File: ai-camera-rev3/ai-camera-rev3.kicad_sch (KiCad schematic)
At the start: 176 parts, among them J1 Conn-01x02_P2mm_NONAME_JST-PH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, J2 TYPE-C-31-M-12, J3 MAXLAB, J4 Conn-02x10_P2.54mm_B-2100S20P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, J5 Conn-01x02_P1.25mm_10114829-1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, J6 Conn_01x24_FFC_0.5mm_AFC01-S2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, Q1 2N7002, Q10 2N7002, Q2 2N7002, Q3 AO3401A, Q4 AO3401A, Q5 2N7002, Q6 AO3401A, Q7 2N7002, Q8 AO3401A, Q9 2N7002, SW1 SW_PB_90deg_K2-1102AQ-H4CW-01, SW2 SW_PB_TS-1187A-B-A-B, SW3 SW_PB_TS-1187A-B-A-B, SW4 SW_PB_90deg_K2-1102AQ-H4CW-01, U1 TP4057-42-SOT26-R, U10 ESP32-S3-WROOM-1-N16R8, U11 MT9284-28J, U12 LTR-303ALS-01, U2 XC6206-2.8V, U3 PCF85063AT_SO8, U4 SOT-23-6_SN74LVC1G373DBVR_TI, U5 SY8089AAAC, U6 PIR_AS312, U7 XC6206-2.8V, U8 RT9166-12GVL, U9 AP1511B, Y1 32.768kHz_Q13FC1350000400

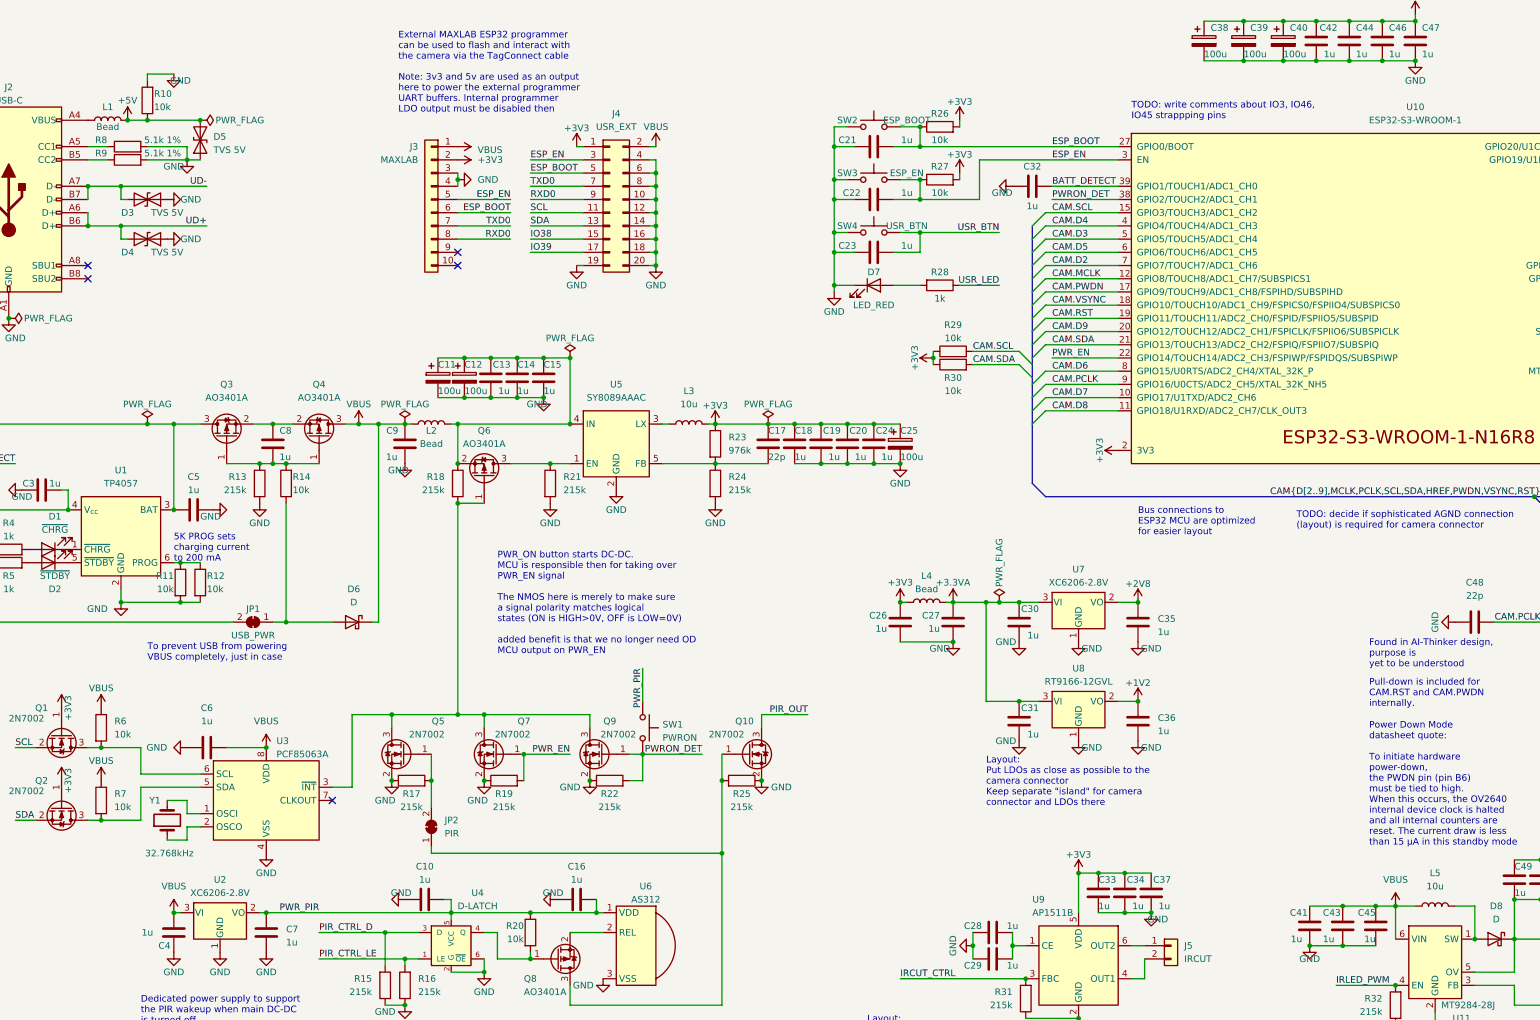
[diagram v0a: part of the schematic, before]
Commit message: EAC-60: rev3: fix all errors and warnings from 7.0.2 KiCAD, update to newer KIML
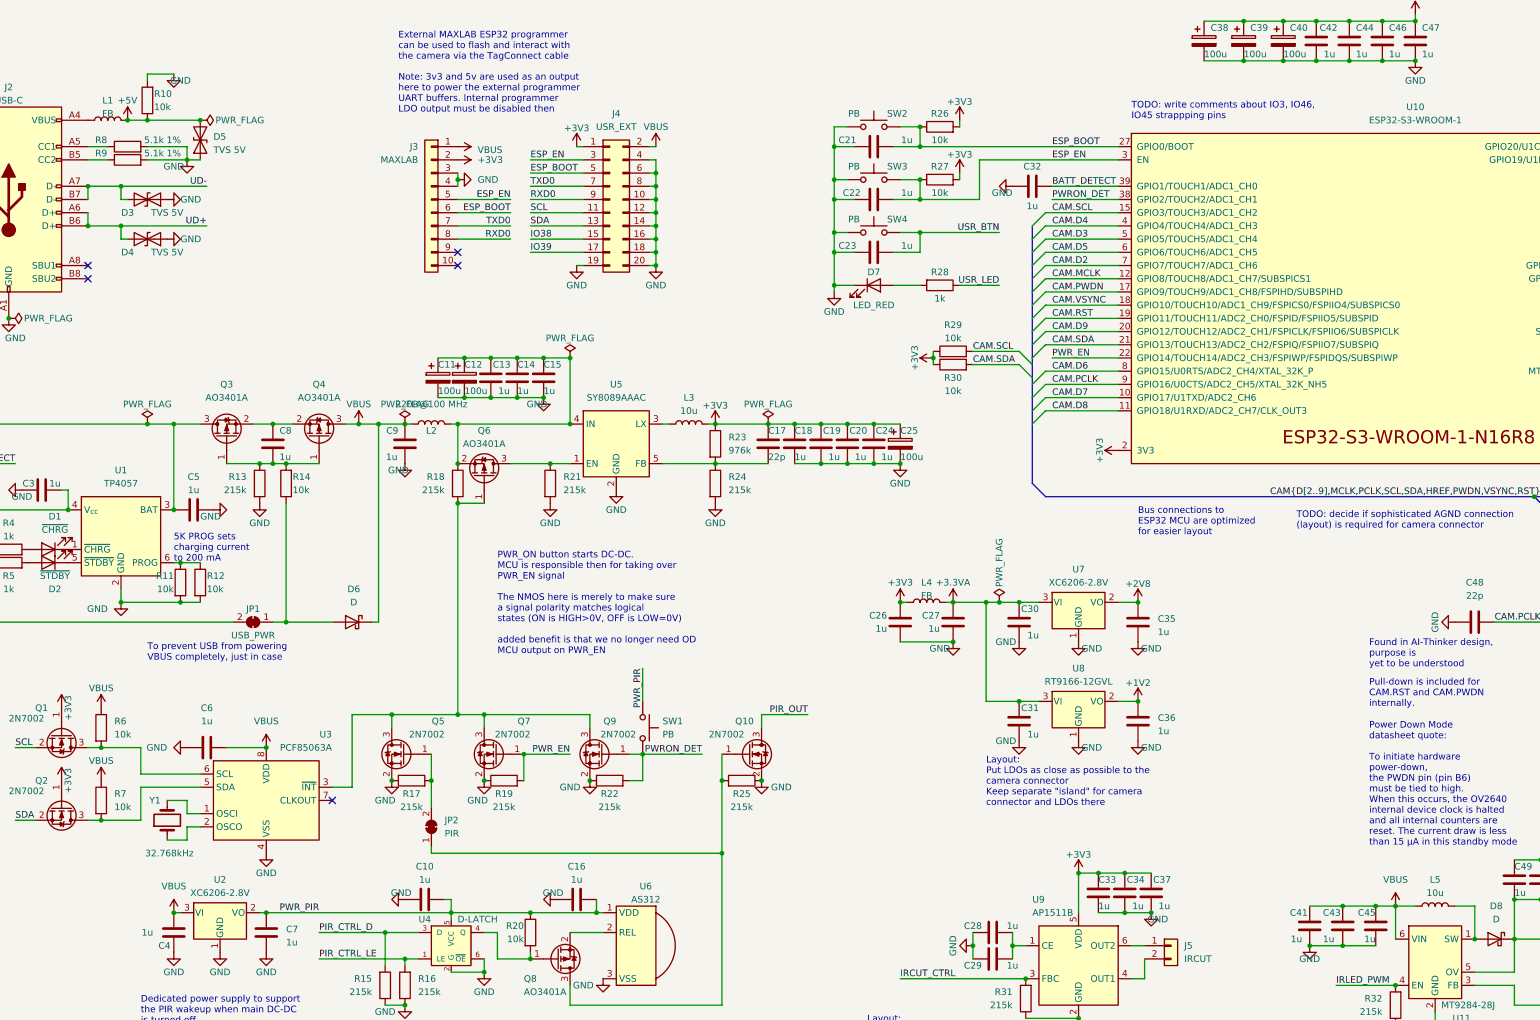
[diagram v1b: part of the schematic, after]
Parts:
- D6, D8: Rating (none) -> 1A
- L1, L4: value 0805_FB_220R@100MHz_BLM21PG221SN1D -> FB_2A_0805_220R@100MHz_BLM21PG221SN1D; symbol 00-kiml-inductors:0805_FB_220R@100MHz_BLM21PG221SN1D -> 00-kiml-inductors:FB_2A_0805_220R@100MHz_BLM21PG221SN1D; UserValue Bead -> FB
- L2: value 0805_FB_220R@100MHz_BLM21PG221SN1D -> FB_2A_0805_220R@100MHz_BLM21PG221SN1D; symbol 00-kiml-inductors:0805_FB_220R@100MHz_BLM21PG221SN1D -> 00-kiml-inductors:FB_2A_0805_220R@100MHz_BLM21PG221SN1D; UserValue Bead -> 220R@100 MHz
- L3, L5: value 10u_SWPA4030S100MT -> 10u_1.5A_4x4mm_SWPA4030S100MT; symbol 00-kiml-inductors:10u_SWPA4030S100MT -> 00-kiml-inductors:10u_1.5A_4x4mm_SWPA4030S100MT; DCR (none) -> 130m; ESR 130m -> (none)
- Q1, Q10, Q2, Q5, Q7, Q9: MFR Jiangsu -> JCET
- SW1: footprint 00-kiml-button-switch-tht:SW_PB_90deg_K2-1102AQ-H4CW-01 -> 00-kiml-switch-button-tht:SW_PB_90deg_K2-1102AQ-H4CW-01; symbol 00-kiml-button-switch-tht:SW_PB_90deg_K2-1102AQ-H4CW-01 -> 00-kiml-switch-button-tht:SW_PB_90deg_K2-1102AQ-H4CW-01; UserValue PWRON -> PB
- SW2: symbol 00-kiml-button-switch-smd:SW_PB_TS-1187A-B-A-B -> 00-kiml-switch-button-smd:SW_PB_TS-1187A-B-A-B; UserValue ESP_BOOT -> PB
- SW3: symbol 00-kiml-button-switch-smd:SW_PB_TS-1187A-B-A-B -> 00-kiml-switch-button-smd:SW_PB_TS-1187A-B-A-B; UserValue ESP_EN -> PB
- SW4: footprint 00-kiml-button-switch-tht:SW_PB_90deg_K2-1102AQ-H4CW-01 -> 00-kiml-switch-button-tht:SW_PB_90deg_K2-1102AQ-H4CW-01; symbol 00-kiml-button-switch-tht:SW_PB_90deg_K2-1102AQ-H4CW-01 -> 00-kiml-switch-button-tht:SW_PB_90deg_K2-1102AQ-H4CW-01; UserValue USR_BTN -> PB
- U12: LNK1 https://lcsc.com/product-detail/Ambient-Light-Sensors_Lite-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 -> https://www.lcsc.com/product-detail/Ambient-Light-Sensors_L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
- U3: value PCF85063AT_SO8 -> PCF85063AT; symbol 00-kiml-timer-rtc:PCF85063AT_SO8 -> 00-kiml-timer-rtc:PCF85063AT/AAZ; MPN PCF85063ATL/1,118 -> PCF85063AT/AAZ
- U4: value SOT-23-6_SN74LVC1G373DBVR_TI -> TI_SN74LVC1G373DBVR; symbol 00-kiml-74xGxx:SOT-23-6_SN74LVC1G373DBVR_TI -> 00-kiml-74xGxx:TI_SN74LVC1G373DBVR

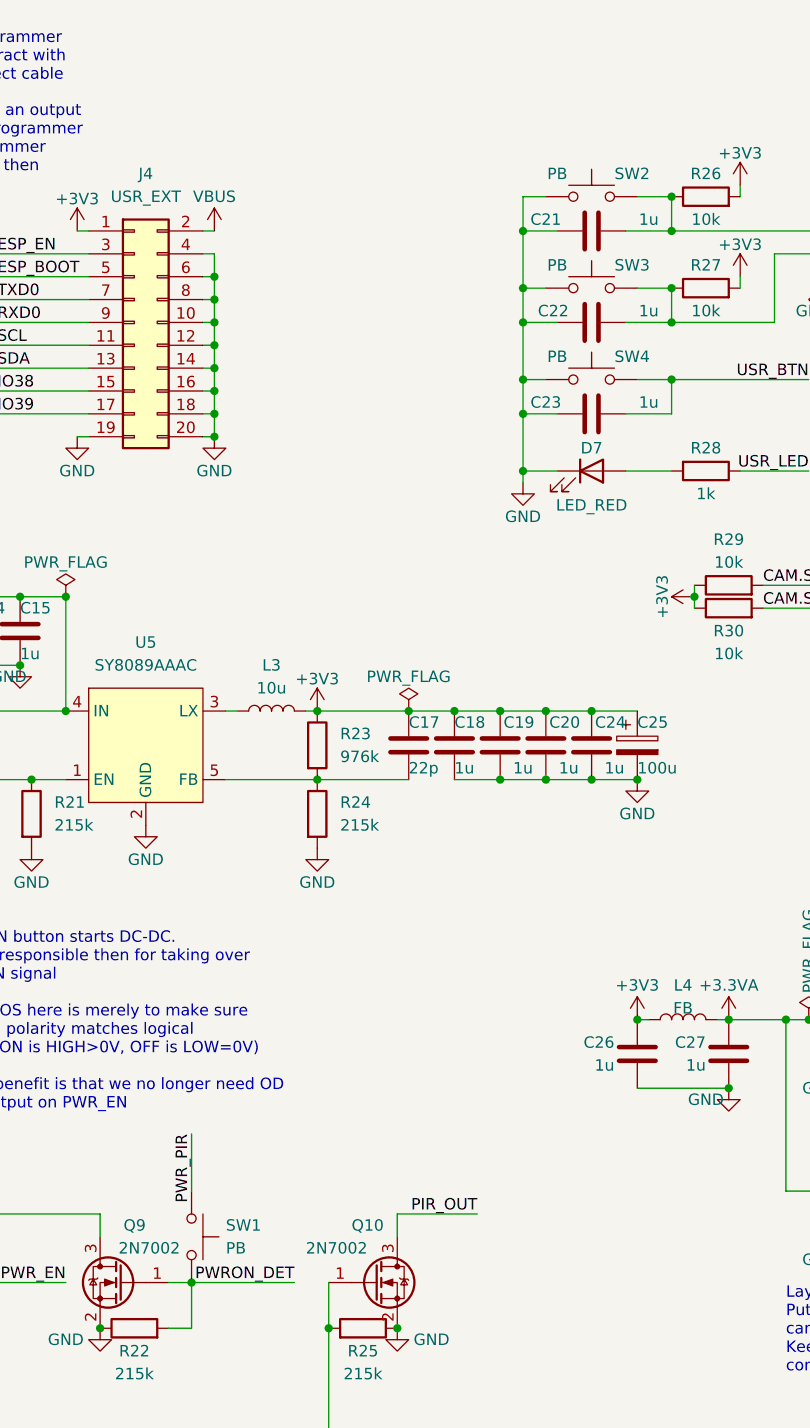
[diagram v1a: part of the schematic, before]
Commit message: EAC-60: rev3: use proper buttons and update KIML reference
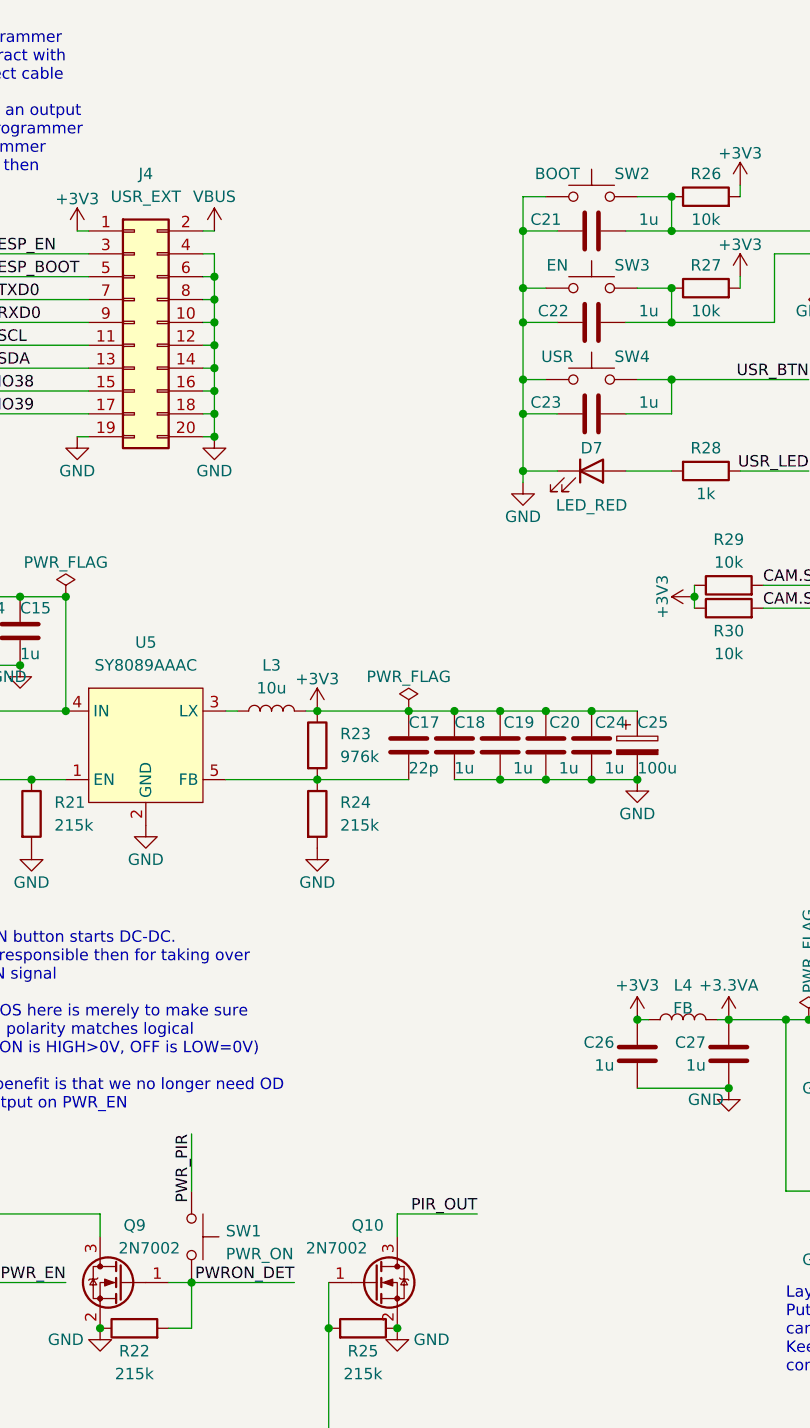
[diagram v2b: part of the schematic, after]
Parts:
- SW1: symbol 00-kiml-switch-button-tht:SW_PB_90deg_K2-1102AQ-H4CW-01 -> 00-kiml-switch-button-tht:SW_PB_90deg_K2-1102AQ-N4CW-01; MPN K2-1102AQ-H4CW-01 -> K2-1102AQ-N4CW-01; SPN1 C961738 -> C338650; UserValue PB -> PWR_ON
- SW2: UserValue PB -> BOOT
- SW3: UserValue PB -> EN
- SW4: symbol 00-kiml-switch-button-tht:SW_PB_90deg_K2-1102AQ-H4CW-01 -> 00-kiml-switch-button-tht:SW_PB_90deg_K2-1102AQ-N4CW-01; MPN K2-1102AQ-H4CW-01 -> K2-1102AQ-N4CW-01; SPN1 C961738 -> C338650; UserValue PB -> USR
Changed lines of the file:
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@@
       (effects (font (size 1.27 1.27)) hide)
     )
-    (property "UserValue" "PB" (at 217.17 41.91 0)
+    (property "UserValue" "BOOT" (at 217.17 41.91 0)
       (effects (font (size 1.27 1.27)))
     )
@@
     )
   )
-  (symbol (lib_id "00-kiml-switch-button-tht:SW_PB_90deg_K2-1102AQ-H4CW-01") (at 220.98 64.77 0) (unit 1)
+  (symbol (lib_id "00-kiml-switch-button-tht:SW_PB_90deg_K2-1102AQ-N4CW-01") (at 220.98 64.77 0) (unit 1)
     (in_bom yes) (on_board yes) (dnp no)
     (property "Reference" "SW4" (at 223.52 62.23 0)
@@
       (effects (font (size 1.27 1.27)) hide)
     )
-    (property "UserValue" "PB" (at 217.17 62.23 0)
+    (property "UserValue" "USR" (at 217.17 62.23 0)
       (effects (font (size 1.27 1.27)))
     )
@@
       (effects (font (size 1.27 1.27)) hide)
     )
-    (property "MPN" "K2-1102AQ-H4CW-01" (at 220.98 76.2 0)
+    (property "MPN" "K2-1102AQ-N4CW-01" (at 220.98 76.2 0)
       (effects (font (size 1.27 1.27)) hide)
     )
@@
       (effects (font (size 1.27 1.27)) hide)
     )
-    (property "SPN1" "C961738" (at 220.98 81.28 0)
+    (property "SPN1" "C338650" (at 220.98 81.28 0)
       (effects (font (size 1.27 1.27)) hide)
     )
@@
       (effects (font (size 1.27 1.27)) hide)
     )
-    (property "UserValue" "PB" (at 217.17 52.07 0)
+    (property "UserValue" "EN" (at 217.17 52.07 0)
       (effects (font (size 1.27 1.27)))
     )
@@
     )
   )
-  (symbol (lib_id "00-kiml-switch-button-tht:SW_PB_90deg_K2-1102AQ-H4CW-01") (at 176.53 160.02 270) (unit 1)
+  (symbol (lib_id "00-kiml-switch-button-tht:SW_PB_90deg_K2-1102AQ-N4CW-01") (at 176.53 160.02 270) (unit 1)
     (in_bom yes) (on_board yes) (dnp no) (fields_autoplaced)
-    (property "Reference" "SW1" (at 180.34 158.75 90)
+    (property "Reference" "SW1" (at 180.34 159.385 90)
       (effects (font (size 1.27 1.27)) (justify left))
     )
@@
       (effects (font (size 1.27 1.27)) hide)
     )
-    (property "UserValue" "PB" (at 180.34 161.29 90)
+    (property "UserValue" "PWR_ON" (at 180.34 161.925 90)
       (effects (font (size 1.27 1.27)) (justify left))
     )
@@
       (effects (font (size 1.27 1.27)) hide)
     )
-    (property "MPN" "K2-1102AQ-H4CW-01" (at 165.1 160.02 0)
+    (property "MPN" "K2-1102AQ-N4CW-01" (at 165.1 160.02 0)
       (effects (font (size 1.27 1.27)) hide)
     )
@@
       (effects (font (size 1.27 1.27)) hide)
     )
-    (property "SPN1" "C961738" (at 160.02 160.02 0)
+    (property "SPN1" "C338650" (at 160.02 160.02 0)
       (effects (font (size 1.27 1.27)) hide)
     )
